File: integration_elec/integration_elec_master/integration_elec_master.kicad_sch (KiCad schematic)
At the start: 0 parts

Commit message: jte touche
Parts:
- added R1: 69k, Resistor_SMD:R_0805_2012Metric_Pad1.20x1.40mm_HandSolder, symbol Device:R_US
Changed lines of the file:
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@@
 	(generator_version "9.0")
 	(paper "A4")
+	(symbol
+		(lib_id "Device:R_US")
+		(at 64.77 128.27 0)
+		(unit 1)
+		(exclude_from_sim no)
+		(in_bom yes)
+		(on_board yes)
+		(dnp no)
+		(fields_autoplaced yes)
+		(property "Reference" "R1"
+			(at 67.31 126.9999 0)
+			(effects
+				(font
+					(size 1.27 1.27)
+				)
+				(justify left)
+			)
+		)
+		(property "Value" "69k"
+			(at 67.31 129.5399 0)
+			(effects
+				(font
+					(size 1.27 1.27)
+				)
+				(justify left)
+			)
+		)
+		(property "Footprint" "Resistor_SMD:R_0805_2012Metric_Pad1.20x1.40mm_HandSolder"
+			(at 65.786 128.524 90)
+			(effects
+				(font
+					(size 1.27 1.27)
+				)
+				(hide yes)
+			)
+		)
+		(property "Datasheet" "~"
+			(at 64.77 128.27 0)
+			(effects
+				(font
+					(size 1.27 1.27)
+				)
+				(hide yes)
+			)
+		)
+		(property "Description" "Resistor, US symbol"
+			(at 64.77 128.27 0)
+			(effects
+				(font
+					(size 1.27 1.27)
+				)
+				(hide yes)
+			)
+		)
+		(property "DigiKey" "311-0.0JRCT-ND"
+			(at 64.77 128.27 0)
+			(effects
+				(font
+					(size 1.27 1.27)
+				)
+				(hide yes)
+			)
+		)
+		(pin "2"
+		)
+		(pin "1"
+		)
+		(instances
+			(project ""
+				(path "/7d904e0d-c2b1-4329-81a9-fc34d181a4fe"
+					(reference "R1")
+					(unit 1)
+				)
+			)
+		)
+	)
 	(sheet_instances
 		(path "/"

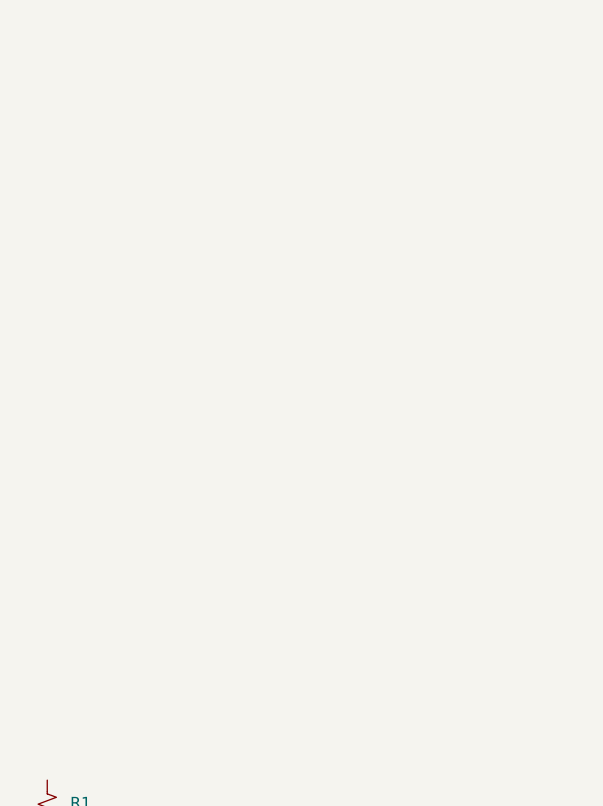
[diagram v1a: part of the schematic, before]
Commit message: EM - Ajout des schématiques XBEE, pas implémenté les footprints encore
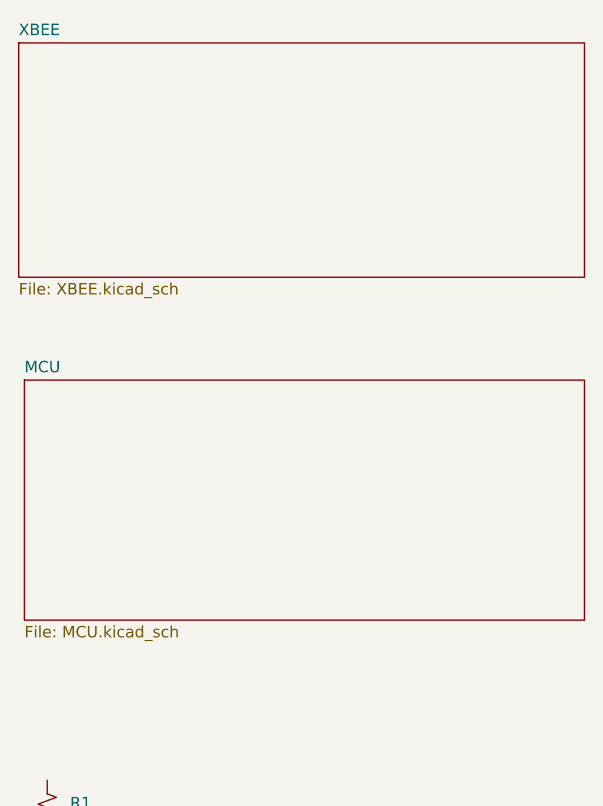
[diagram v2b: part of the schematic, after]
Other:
- added sheet MCU (MCU.kicad_sch)
- added sheet XBEE (XBEE.kicad_sch)
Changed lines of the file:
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@@
+		)
+	)
+	(sheet
+		(at 62.23 80.01)
+		(size 62.23 26.67)
+		(exclude_from_sim no)
+		(in_bom yes)
+		(on_board yes)
+		(dnp no)
+		(fields_autoplaced yes)
+		(stroke
+			(width 0.1524)
+			(type solid)
+		)
+		(fill
+			(color 0 0 0 0.0000)
+		)
+		(property "Sheetname" "MCU"
+			(at 62.23 79.2984 0)
+			(effects
+				(font
+					(size 1.27 1.27)
+				)
+				(justify left bottom)
+			)
+		)
+		(property "Sheetfile" "MCU.kicad_sch"
+			(at 62.23 107.2646 0)
+			(effects
+				(font
+					(size 1.27 1.27)
+				)
+				(justify left top)
+			)
+		)
+		(instances
+			(project "integration_elec_master"
+				(path "/7d904e0d-c2b1-4329-81a9-fc34d181a4fe"
+					(page "3")
+				)
+			)
+		)
+	)
+	(sheet
+		(at 61.595 42.545)
+		(size 62.865 26.035)
+		(exclude_from_sim no)
+		(in_bom yes)
+		(on_board yes)
+		(dnp no)
+		(fields_autoplaced yes)
+		(stroke
+			(width 0.1524)
+			(type solid)
+		)
+		(fill
+			(color 0 0 0 0.0000)
+		)
+		(property "Sheetname" "XBEE"
+			(at 61.595 41.8334 0)
+			(effects
+				(font
+					(size 1.27 1.27)
+				)
+				(justify left bottom)
+			)
+		)
+		(property "Sheetfile" "XBEE.kicad_sch"
+			(at 61.595 69.1646 0)
+			(effects
+				(font
+					(size 1.27 1.27)
+				)
+				(justify left top)
+			)
+		)
+		(instances
+			(project "integration_elec_master"
+				(path "/7d904e0d-c2b1-4329-81a9-fc34d181a4fe"
+					(page "2")
+				)
+			)
 		)
 	)

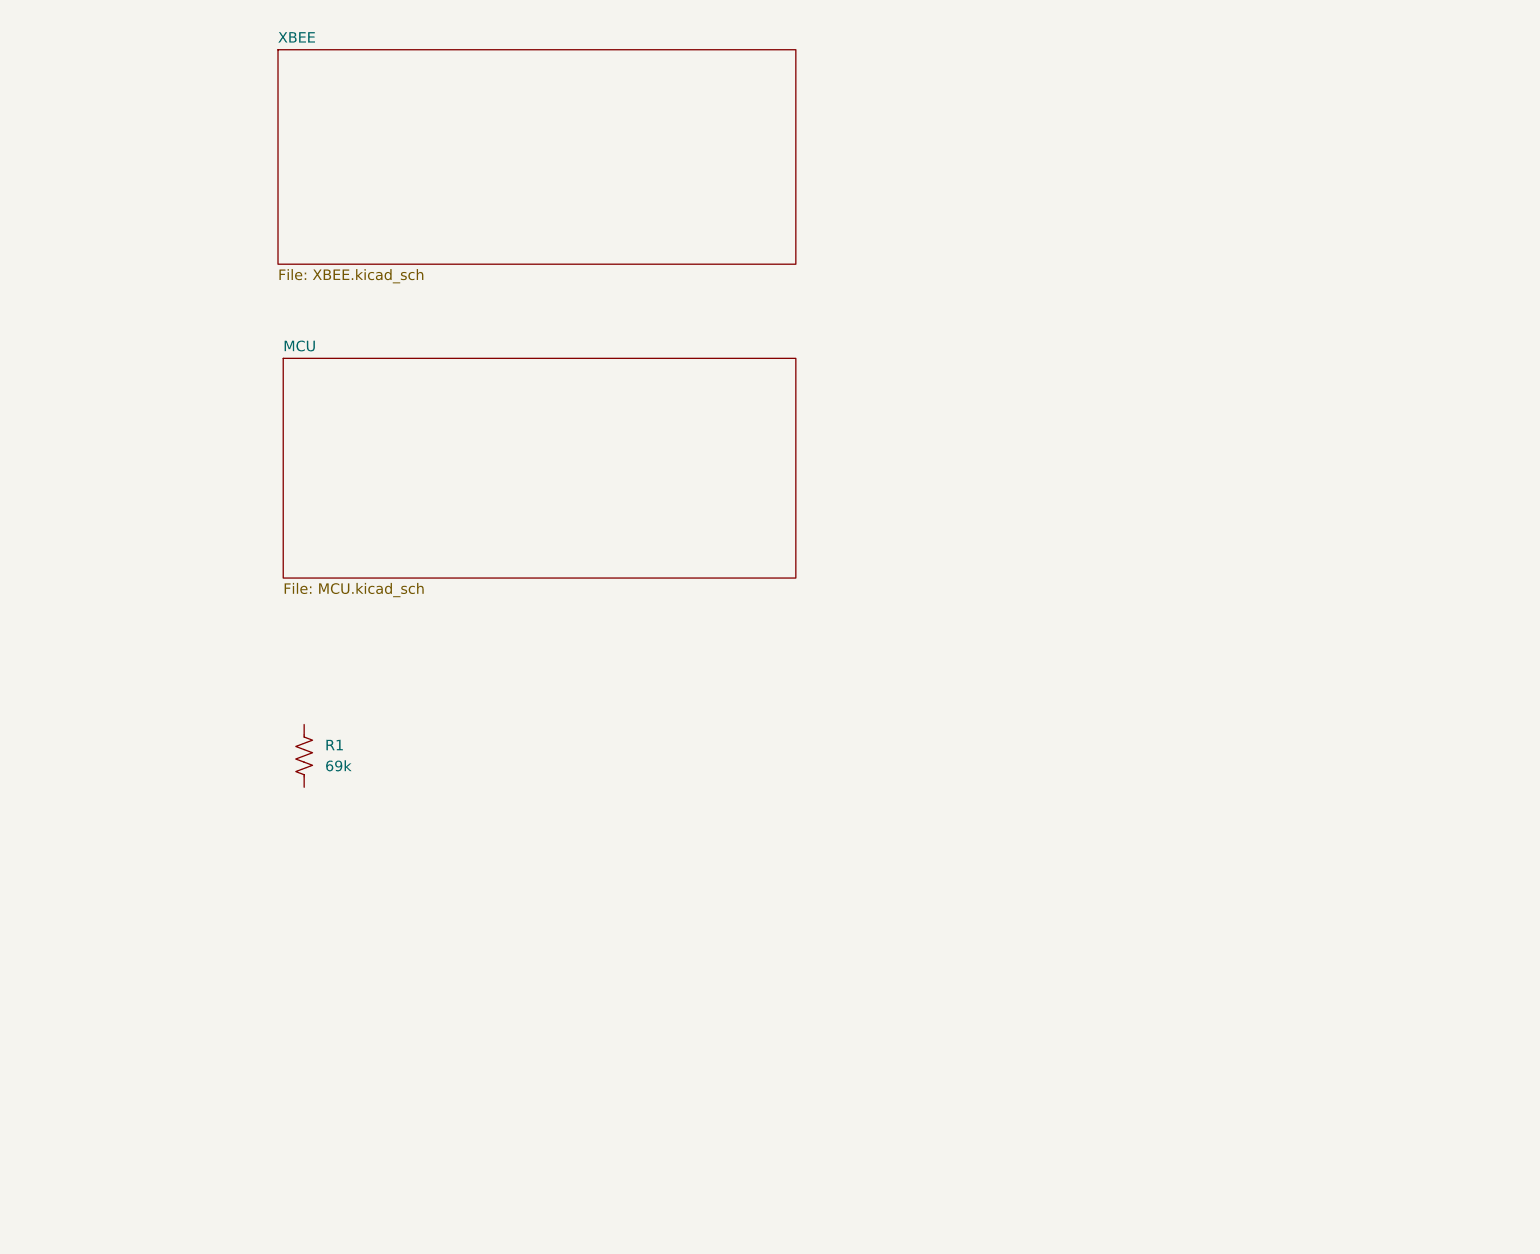
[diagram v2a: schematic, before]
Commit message: EM - Ajout des pages hiérarchiques pour le master, next : ajouter connecteurs pour les capteurs
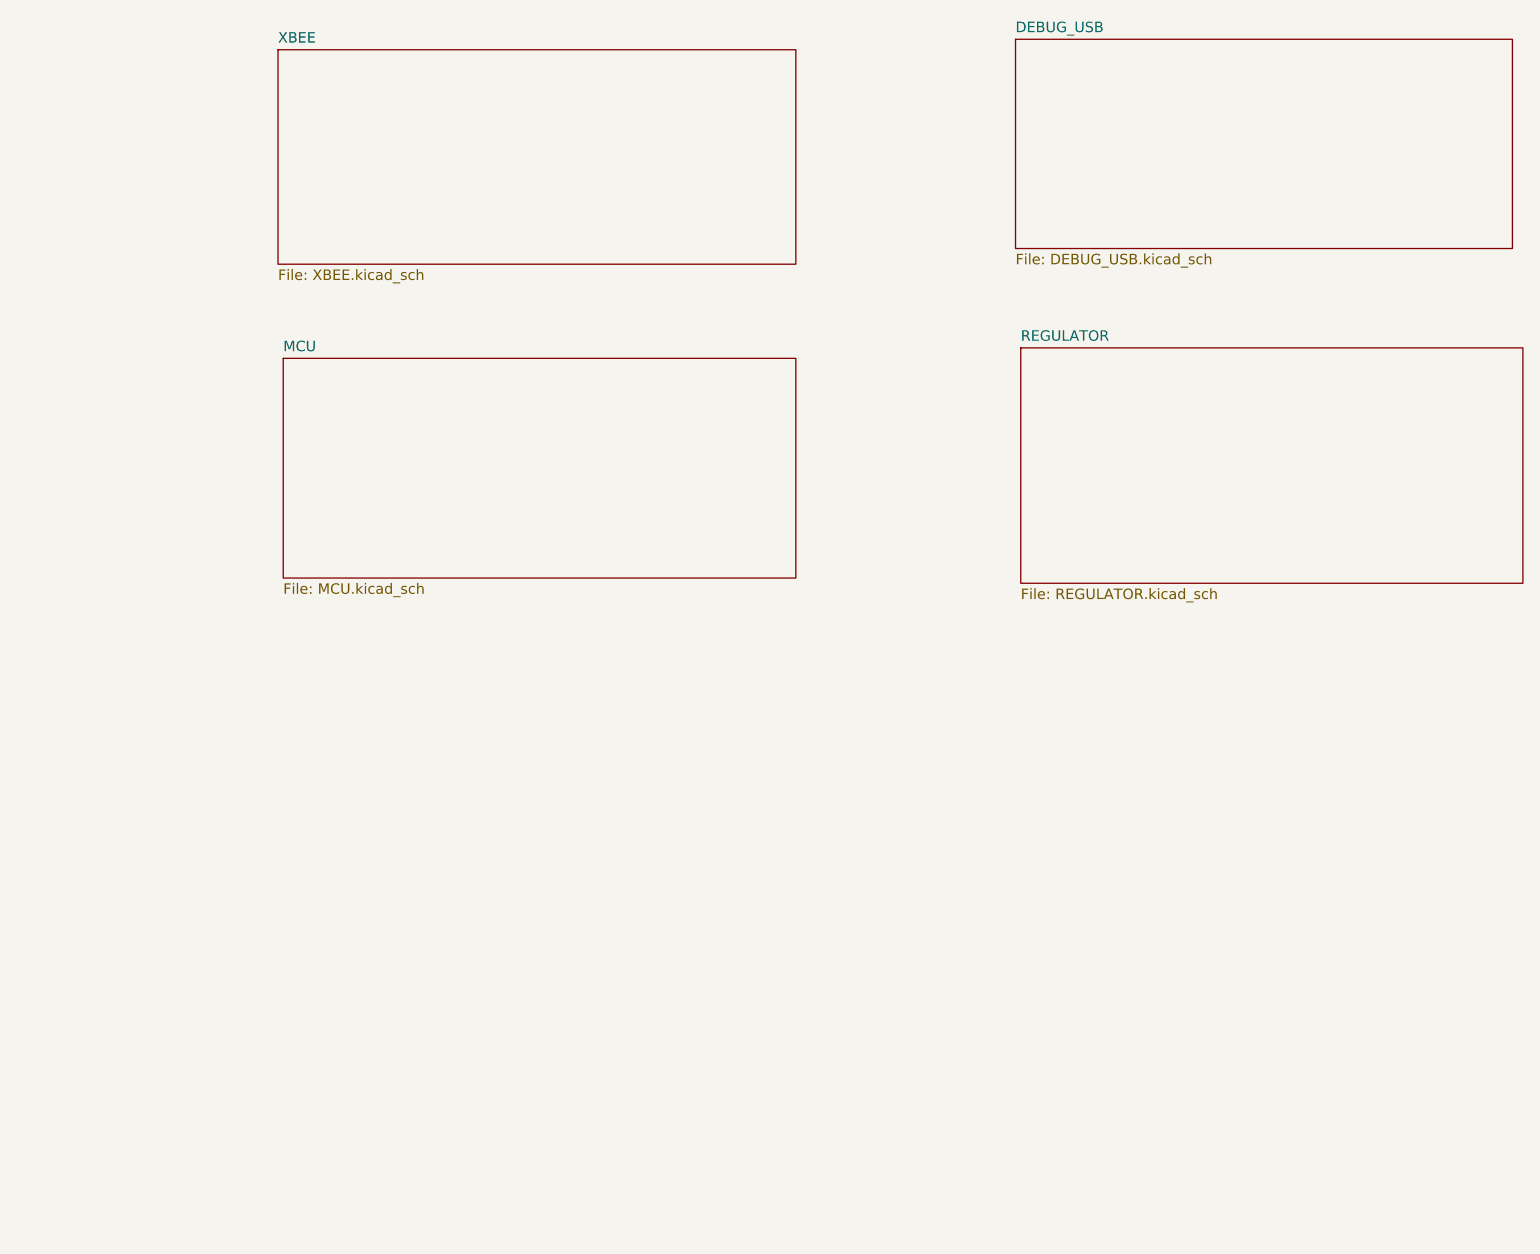
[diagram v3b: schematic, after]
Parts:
- removed R1: 69k, Resistor_SMD:R_0805_2012Metric_Pad1.20x1.40mm_HandSolder, symbol Device:R_US
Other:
- added sheet DEBUG_USB (DEBUG_USB.kicad_sch)
- added sheet REGULATOR (REGULATOR.kicad_sch)
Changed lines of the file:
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@@
 	(generator_version "9.0")
 	(paper "A4")
-	(symbol
-		(lib_id "Device:R_US")
-		(at 64.77 128.27 0)
-		(unit 1)
-		(exclude_from_sim no)
-		(in_bom yes)
-		(on_board yes)
-		(dnp no)
-		(fields_autoplaced yes)
-		(property "Reference" "R1"
-			(at 67.31 126.9999 0)
-			(effects
-				(font
-					(size 1.27 1.27)
-				)
-				(justify left)
-			)
-		)
-		(property "Value" "69k"
-			(at 67.31 129.5399 0)
-			(effects
-				(font
-					(size 1.27 1.27)
-				)
-				(justify left)
-			)
-		)
-		(property "Footprint" "Resistor_SMD:R_0805_2012Metric_Pad1.20x1.40mm_HandSolder"
-			(at 65.786 128.524 90)
-			(effects
-				(font
-					(size 1.27 1.27)
-				)
-				(hide yes)
-			)
-		)
-		(property "Datasheet" "~"
-			(at 64.77 128.27 0)
-			(effects
-				(font
-					(size 1.27 1.27)
-				)
-				(hide yes)
-			)
-		)
-		(property "Description" "Resistor, US symbol"
-			(at 64.77 128.27 0)
-			(effects
-				(font
-					(size 1.27 1.27)
-				)
-				(hide yes)
-			)
-		)
-		(property "DigiKey" "311-0.0JRCT-ND"
-			(at 64.77 128.27 0)
-			(effects
-				(font
-					(size 1.27 1.27)
-				)
-				(hide yes)
-			)
-		)
-		(pin "2"
-		)
-		(pin "1"
-		)
-		(instances
-			(project ""
-				(path "/7d904e0d-c2b1-4329-81a9-fc34d181a4fe"
-					(reference "R1")
-					(unit 1)
-				)
-			)
-		)
-	)
 	(sheet
 		(at 62.23 80.01)
@@
 				)
 			)
+		)
+	)
+	(sheet
+		(at 151.765 78.74)
+		(size 60.96 28.575)
+		(exclude_from_sim no)
+		(in_bom yes)
+		(on_board yes)
+		(dnp no)
+		(fields_autoplaced yes)
+		(stroke
+			(width 0.1524)
+			(type solid)
+		)
+		(fill
+			(color 0 0 0 0.0000)
+		)
+		(property "Sheetname" "REGULATOR"
+			(at 151.765 78.0284 0)
+			(effects
+				(font
+					(size 1.27 1.27)
+				)
+				(justify left bottom)
+			)
+		)
+		(property "Sheetfile" "REGULATOR.kicad_sch"
+			(at 151.765 107.8996 0)
+			(effects
+				(font
+					(size 1.27 1.27)
+				)
+				(justify left top)
+			)
+		)
+		(instances
+			(project "integration_elec_master"
+				(path "/7d904e0d-c2b1-4329-81a9-fc34d181a4fe"
+					(page "5")
+				)
+			)
+		)
+	)
+	(sheet
+		(at 151.13 41.275)
+		(size 60.325 25.4)
+		(exclude_from_sim no)
+		(in_bom yes)
+		(on_board yes)
+		(dnp no)
+		(fields_autoplaced yes)
+		(stroke
+			(width 0.1524)
+			(type solid)
+		)
+		(fill
+			(color 0 0 0 0.0000)
+		)
+		(property "Sheetname" "DEBUG_USB"
+			(at 151.13 40.5634 0)
+			(effects
+				(font
+					(size 1.27 1.27)
+				)
+				(justify left bottom)
+			)
+		)
+		(property "Sheetfile" "DEBUG_USB.kicad_sch"
+			(at 151.13 67.2596 0)
+			(effects
+				(font
+					(size 1.27 1.27)
+				)
+				(justify left top)
+			)
+		)
+		(instances
+			(project "integration_elec_master"
+				(path "/7d904e0d-c2b1-4329-81a9-fc34d181a4fe"
+					(page "4")
+				)
+			)

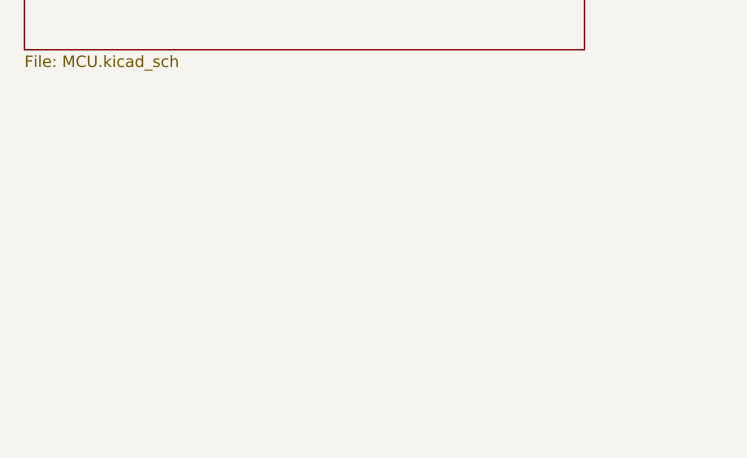
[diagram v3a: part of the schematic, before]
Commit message: Added screen into schematic
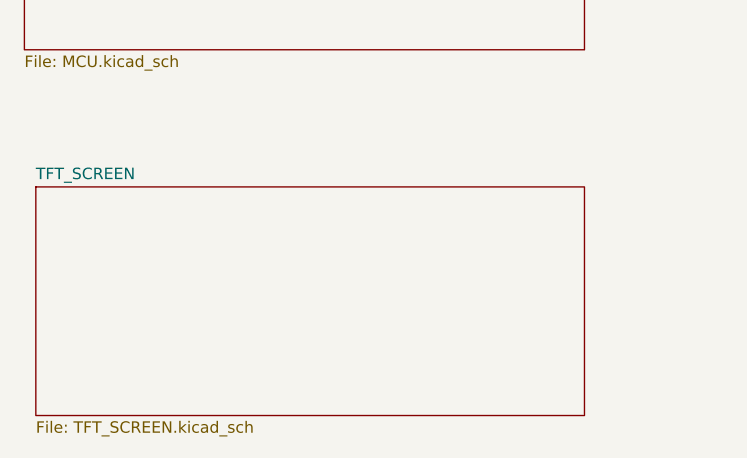
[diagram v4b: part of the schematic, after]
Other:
- added sheet TFT_SCREEN (TFT_SCREEN.kicad_sch)
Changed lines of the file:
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@@
 	(paper "A4")
+	(sheet
+		(at 63.5 121.92)
+		(size 60.96 25.4)
+		(exclude_from_sim no)
+		(in_bom yes)
+		(on_board yes)
+		(dnp no)
+		(fields_autoplaced yes)
+		(stroke
+			(width 0.1524)
+			(type solid)
+		)
+		(fill
+			(color 0 0 0 0.0000)
+		)
+		(property "Sheetname" "TFT_SCREEN"
+			(at 63.5 121.2084 0)
+			(effects
+				(font
+					(size 1.27 1.27)
+				)
+				(justify left bottom)
+			)
+		)
+		(property "Sheetfile" "TFT_SCREEN.kicad_sch"
+			(at 63.5 147.9046 0)
+			(effects
+				(font
+					(size 1.27 1.27)
+				)
+				(justify left top)
+			)
+		)
+		(instances
+			(project "integration_elec_master"
+				(path "/7d904e0d-c2b1-4329-81a9-fc34d181a4fe"
+					(page "6")
+				)
+			)
+		)
+	)
 	(sheet
 		(at 62.23 80.01)

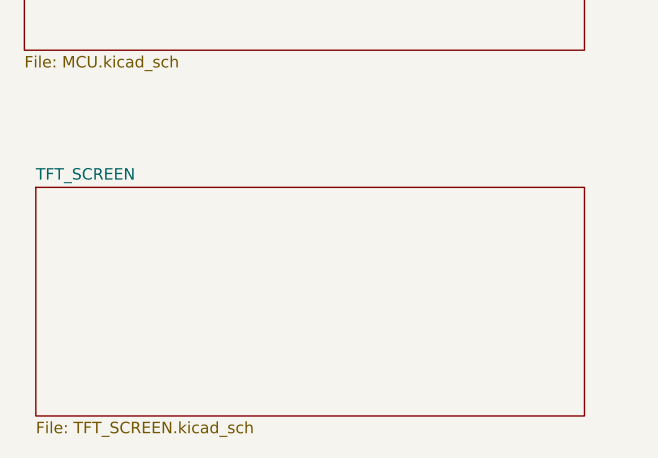
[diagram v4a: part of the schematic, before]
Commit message: Added footprint, symbol, 3D model for joystick. Added schematic for Joystick and comments
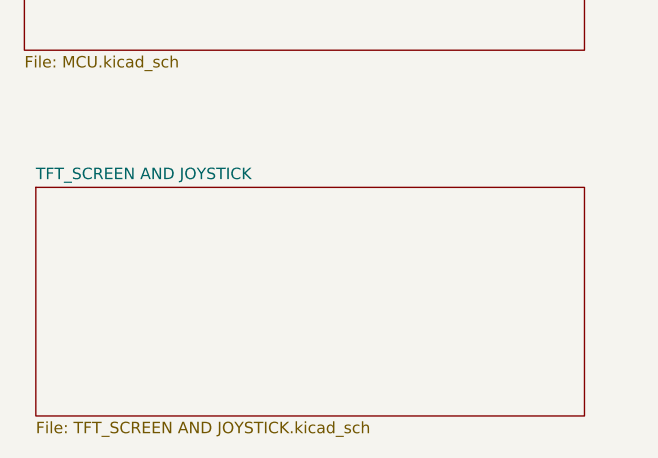
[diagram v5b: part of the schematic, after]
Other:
- sheet TFT_SCREEN renamed TFT_SCREEN AND JOYSTICK
- sheet TFT_SCREEN AND JOYSTICK: file TFT_SCREEN.kicad_sch -> TFT_SCREEN AND JOYSTICK.kicad_sch
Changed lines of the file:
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@@
 		(on_board yes)
 		(dnp no)
-		(fields_autoplaced yes)
 		(stroke
 			(width 0.1524)
@@
 			(color 0 0 0 0.0000)
 		)
-		(property "Sheetname" "TFT_SCREEN"
-			(at 63.5 121.2084 0)
+		(property "Sheetname" "TFT_SCREEN AND JOYSTICK"
+			(at 63.5 121.158 0)
 			(effects
 				(font
@@
 			)
 		)
-		(property "Sheetfile" "TFT_SCREEN.kicad_sch"
+		(property "Sheetfile" "TFT_SCREEN AND JOYSTICK.kicad_sch"
 			(at 63.5 147.9046 0)
 			(effects
